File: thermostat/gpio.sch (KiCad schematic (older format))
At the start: 28 parts

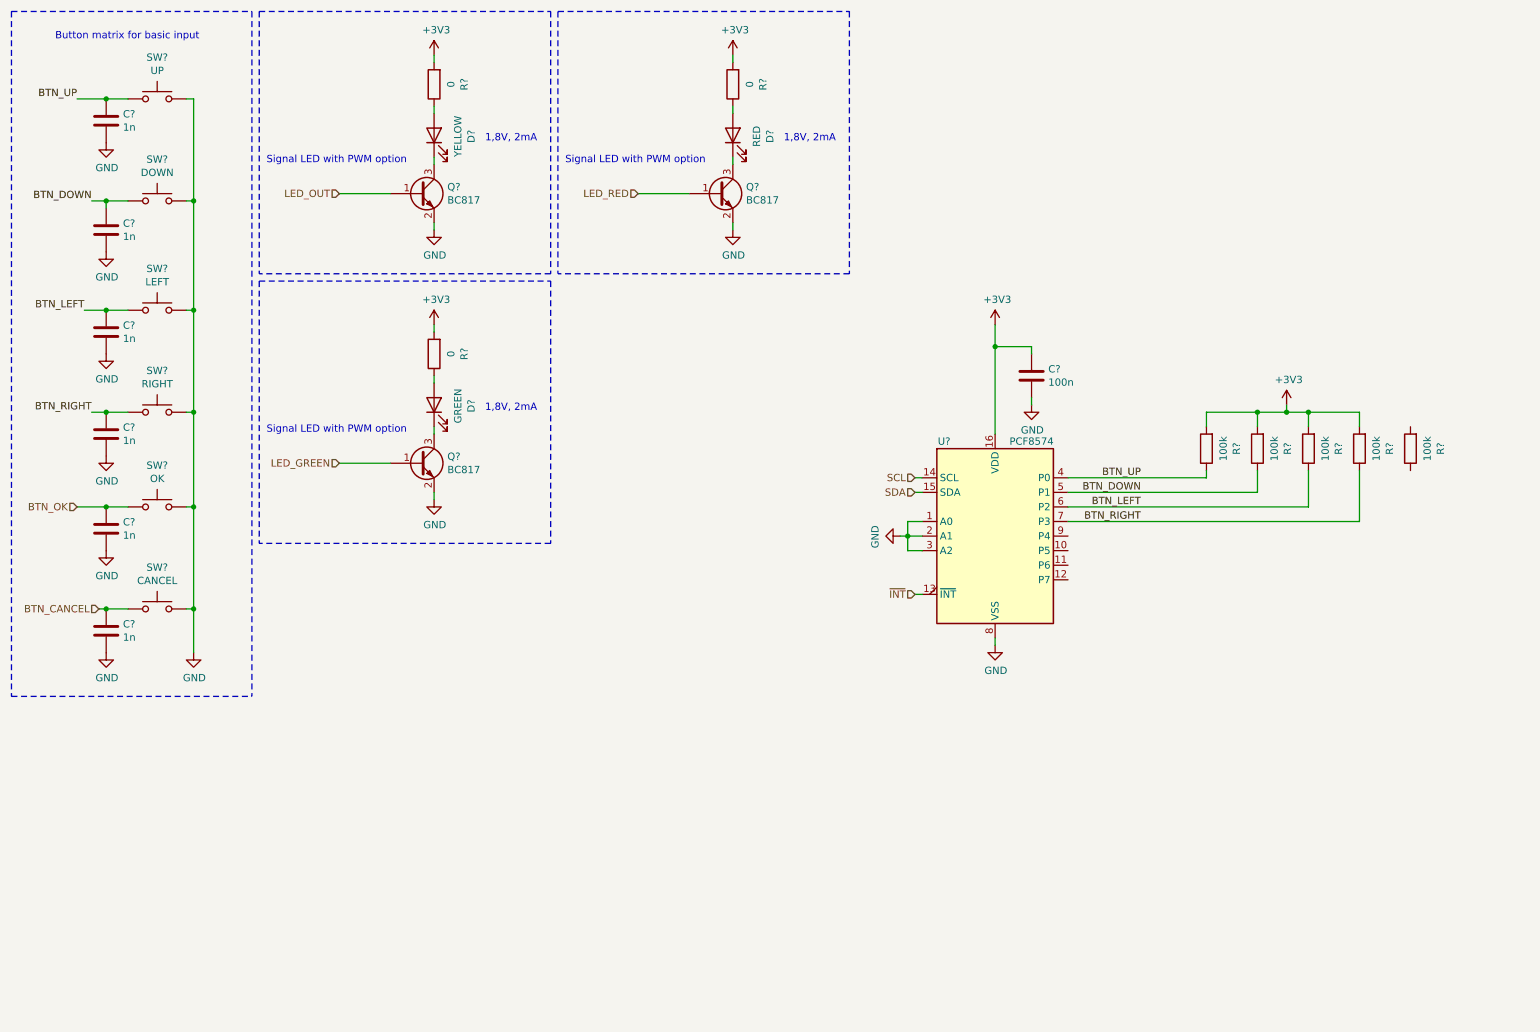
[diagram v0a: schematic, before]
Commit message: Updated symbols after library update, some footprints still need to be assigned. Deleted PCB except for Display and buttons. Button arrangement wrong. Move buttons to other side of Display. Maybe put buttons on separate PCB and create one PCB for MCU and logic, since that needs to be a four layer one. That is expensive and should be kept as small as possible.
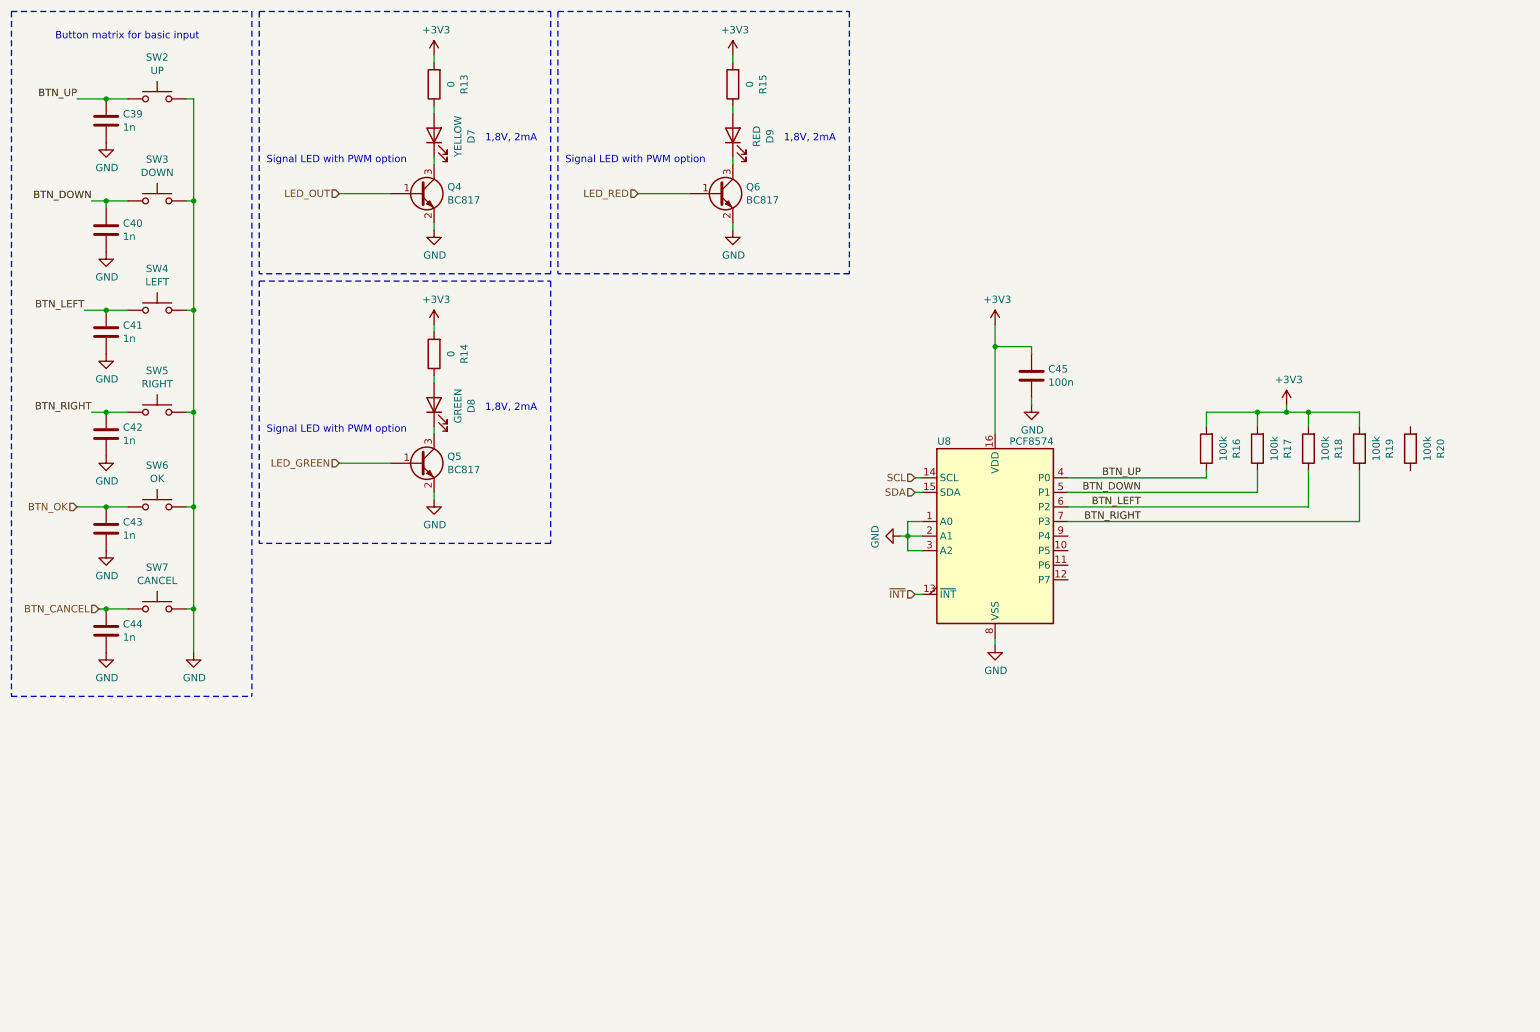
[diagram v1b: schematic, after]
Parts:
- C39, C40, C41, C42, C43, C44, C45: renamed from C?; footprint (none) -> Capacitor_SMD:C_0603_1608Metric
- U8: renamed from U?; footprint (none) -> Package_SO:SOIC-16W_7.5x10.3mm_P1.27mm
- gave numbers to parts that had none: 20

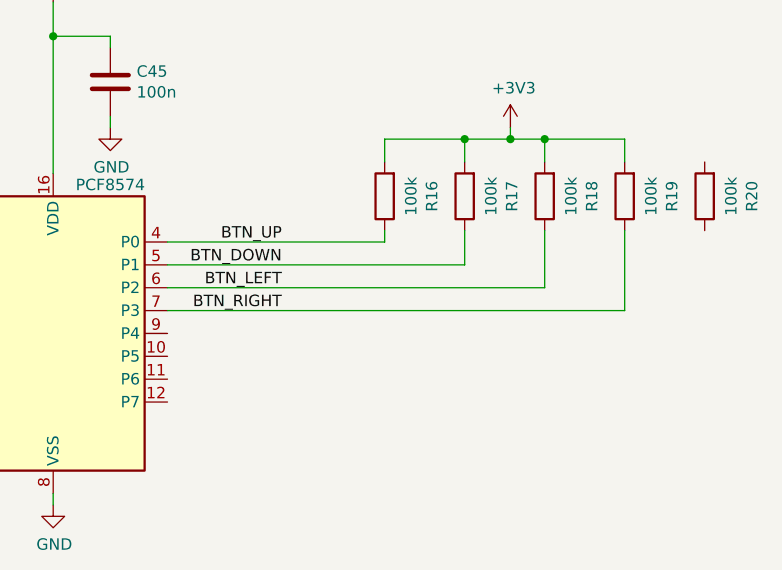
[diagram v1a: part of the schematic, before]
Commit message: Finalized Thermostat circuit based on the MKW41Z.
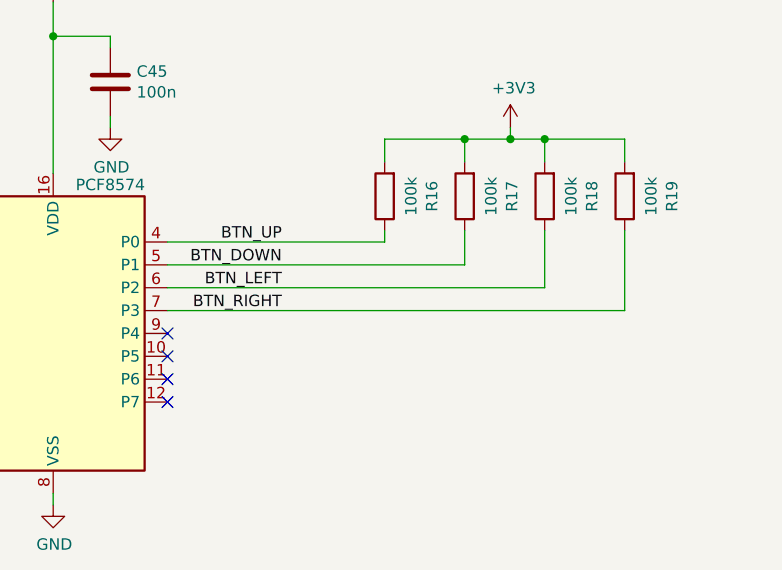
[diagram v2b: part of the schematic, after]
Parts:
- removed R20: 100k, Resistor_SMD:R_0603_1608Metric, symbol Device:R
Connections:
- no-connect marks 0 -> 4
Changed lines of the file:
@@
-	-1   0    0    1
-$EndComp
-$Comp
-L Device:R R?
-U 1 1 5F469953
-P 10250 3600
-AR Path="/5E6A63AE/5F469953" Ref="R?"  Part="1"
-AR Path="/5F469953" Ref="R?"  Part="1"
-AR Path="/5F39C8C1/5F469953" Ref="R20"  Part="1"
-F 0 "R20" V 10043 3600 50  0000 C CNN
-F 1 "100k" V 10134 3600 50  0000 C CNN
-F 2 "Resistor_SMD:R_0603_1608Metric" V 10180 3600 50  0001 C CNN
-F 3 "~" H 10250 3600 50  0001 C CNN
-	1    10250 3600
 	-1   0    0    1
 $EndComp
@@
 Wire Wire Line
 	7400 2900 7400 3500
+NoConn ~ 7900 4200
+NoConn ~ 7900 4300
+NoConn ~ 7900 4400
+NoConn ~ 7900 4500
 $EndSCHEMATC

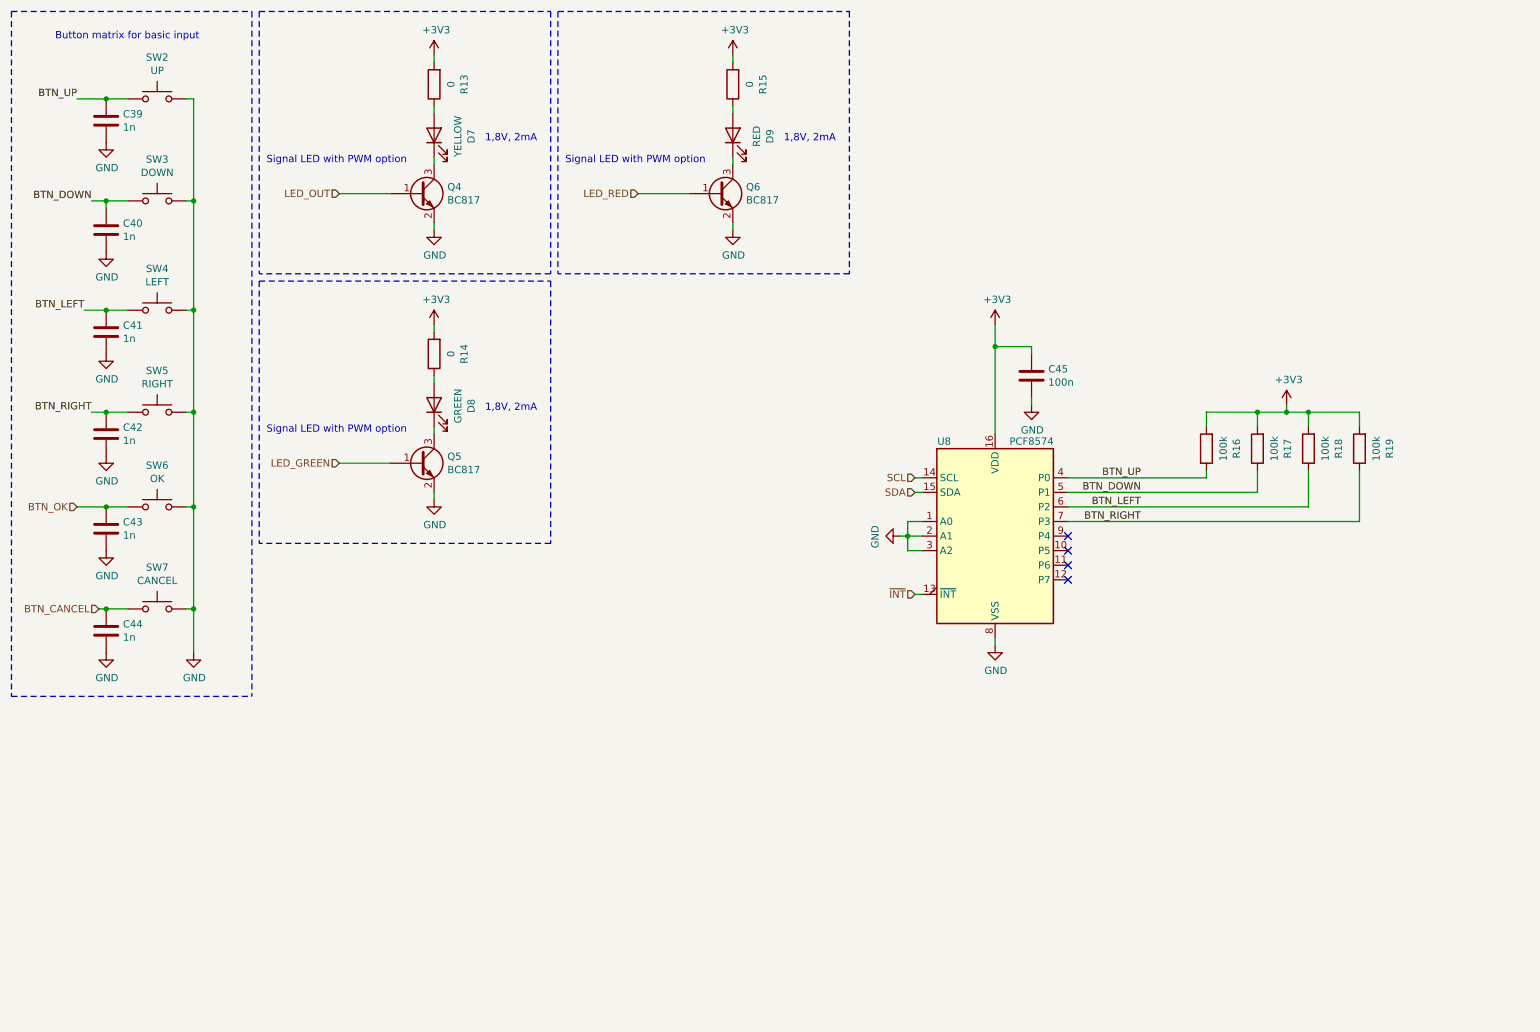
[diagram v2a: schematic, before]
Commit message: Removed buttons and signal LEDs as they should be moved to a separate peripheral board (to save expensive board space on the 4-layer PCB). Added bus transceiver for UART_RX to optionally be able to accept inputs over UART.
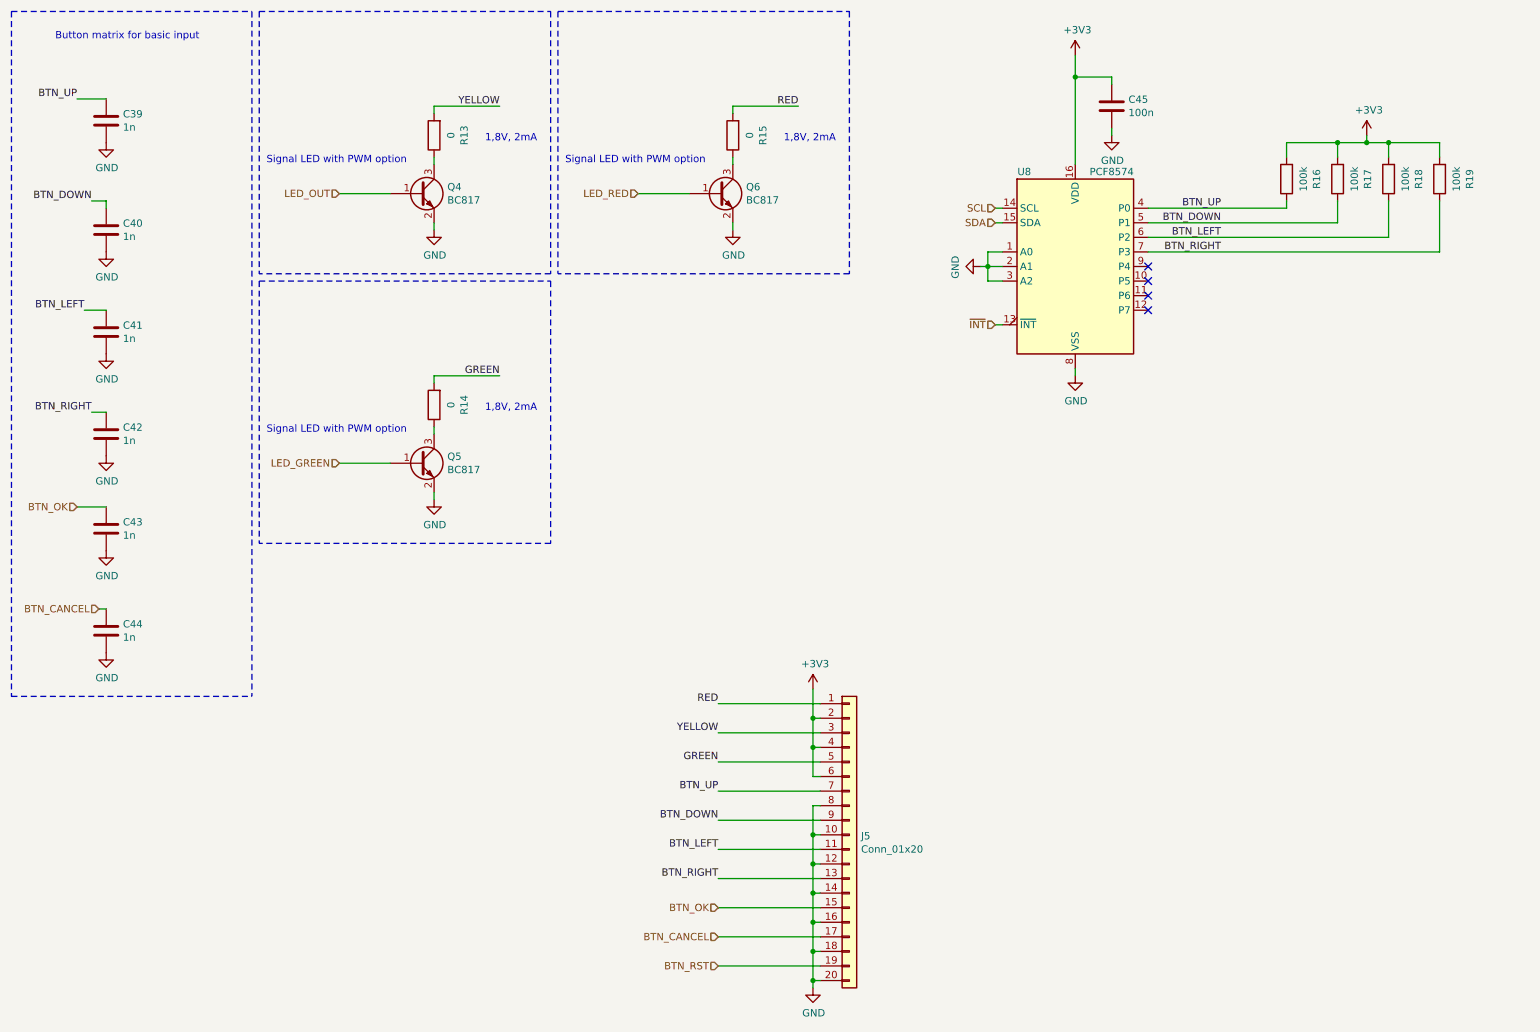
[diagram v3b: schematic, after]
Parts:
- removed D7: YELLOW, LED_SMD:LED_1210_3225Metric, symbol Device:LED
- removed D8: GREEN, LED_SMD:LED_1210_3225Metric, symbol Device:LED
- removed D9: RED, LED_SMD:LED_1210_3225Metric, symbol Device:LED
- removed SW2: UP, Button_Switch_SMD:SW_SPST_Panasonic_EVQPL_3PL_5PL_PT_A08, symbol Switch:SW_Push
- removed SW3: DOWN, Button_Switch_SMD:SW_SPST_Panasonic_EVQPL_3PL_5PL_PT_A08, symbol Switch:SW_Push
- removed SW4: LEFT, Button_Switch_SMD:SW_SPST_Panasonic_EVQPL_3PL_5PL_PT_A08, symbol Switch:SW_Push
- removed SW5: RIGHT, Button_Switch_SMD:SW_SPST_Panasonic_EVQPL_3PL_5PL_PT_A08, symbol Switch:SW_Push
- removed SW6: OK, Button_Switch_SMD:SW_SPST_Panasonic_EVQPL_3PL_5PL_PT_A08, symbol Switch:SW_Push
- removed SW7: CANCEL, Button_Switch_SMD:SW_SPST_Panasonic_EVQPL_3PL_5PL_PT_A08, symbol Switch:SW_Push
- added J5: Conn_01x20, Connector_PinHeader_2.54mm:PinHeader_2x10_P2.54mm_Vertical_SMD, symbol Connector_Generic:Conn_01x20
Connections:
- net +3V3: now also J5.2 (Pin_2), J5.4 (Pin_4), J5.6 (Pin_6); no longer R13.2, R14.2, R15.2
- net BTN_CANCEL: now also J5.17 (Pin_17)
- net BTN_DOWN: now also J5.9 (Pin_9)
- net BTN_LEFT: now also J5.11 (Pin_11)
- net BTN_OK: now also J5.15 (Pin_15)
- net BTN_RIGHT: now also J5.13 (Pin_13)
- net BTN_UP: now also J5.7 (Pin_7)
- net GND: now also J5.10 (Pin_10), J5.12 (Pin_12), J5.14 (Pin_14), J5.16 (Pin_16), J5.18 (Pin_18), J5.20 (Pin_20), J5.8 (Pin_8)
- net at Q4.3 (C): now also R13.1
- net at Q6.3 (C): now also R15.1
- net at Q5.3 (C): now also R14.1
- new net BTN_RST: J5.19 (Pin_19)
- new net GREEN: J5.5 (Pin_5), R14.2
- new net RED: J5.1 (Pin_1), R15.2
- new net YELLOW: J5.3 (Pin_3), R13.2
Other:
- moved on the sheet: C45, R13, R14, R15, R16, R17, R18, R19, U8
